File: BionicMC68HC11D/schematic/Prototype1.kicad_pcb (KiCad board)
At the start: 2 copper layers, 48.3 x 71.1 mm, 16 parts, among them J1 BionicConnector, U1 MC68HC11D0P, U2 74HCT126

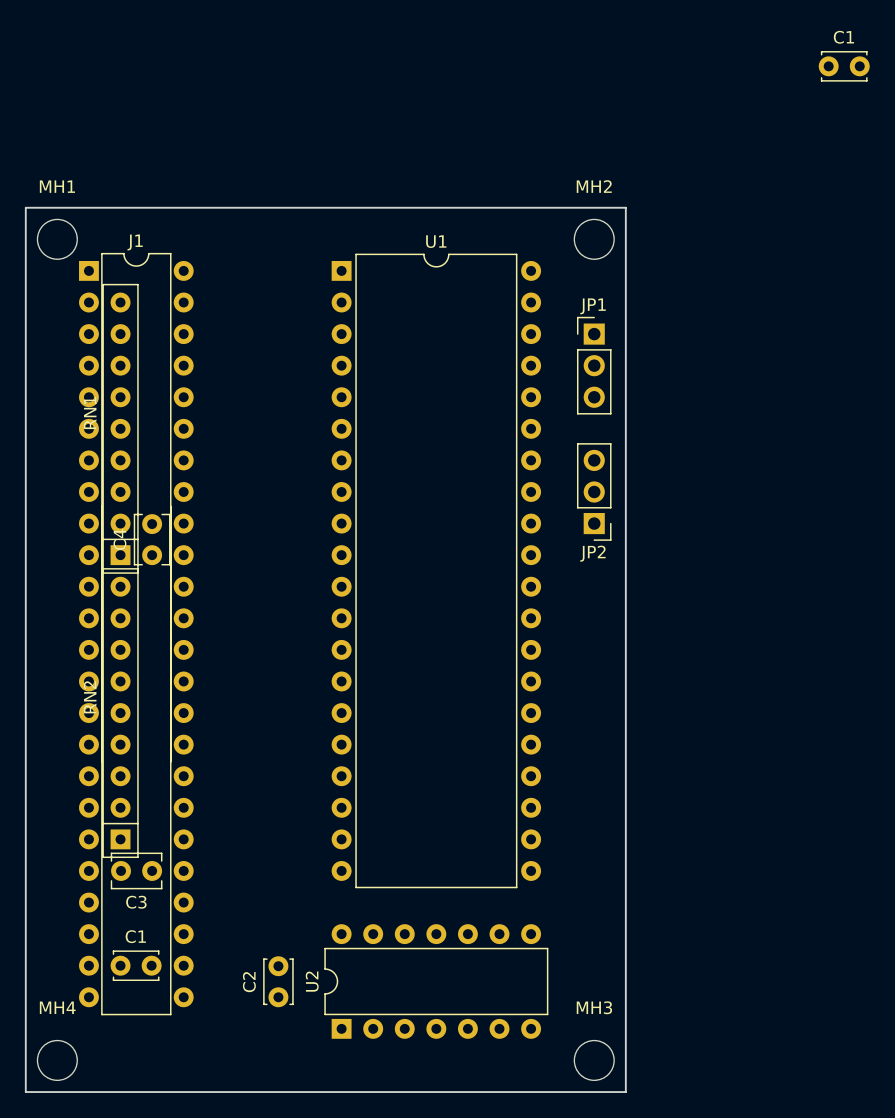
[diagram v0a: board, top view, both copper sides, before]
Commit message: Fix Bionic connector pin outs
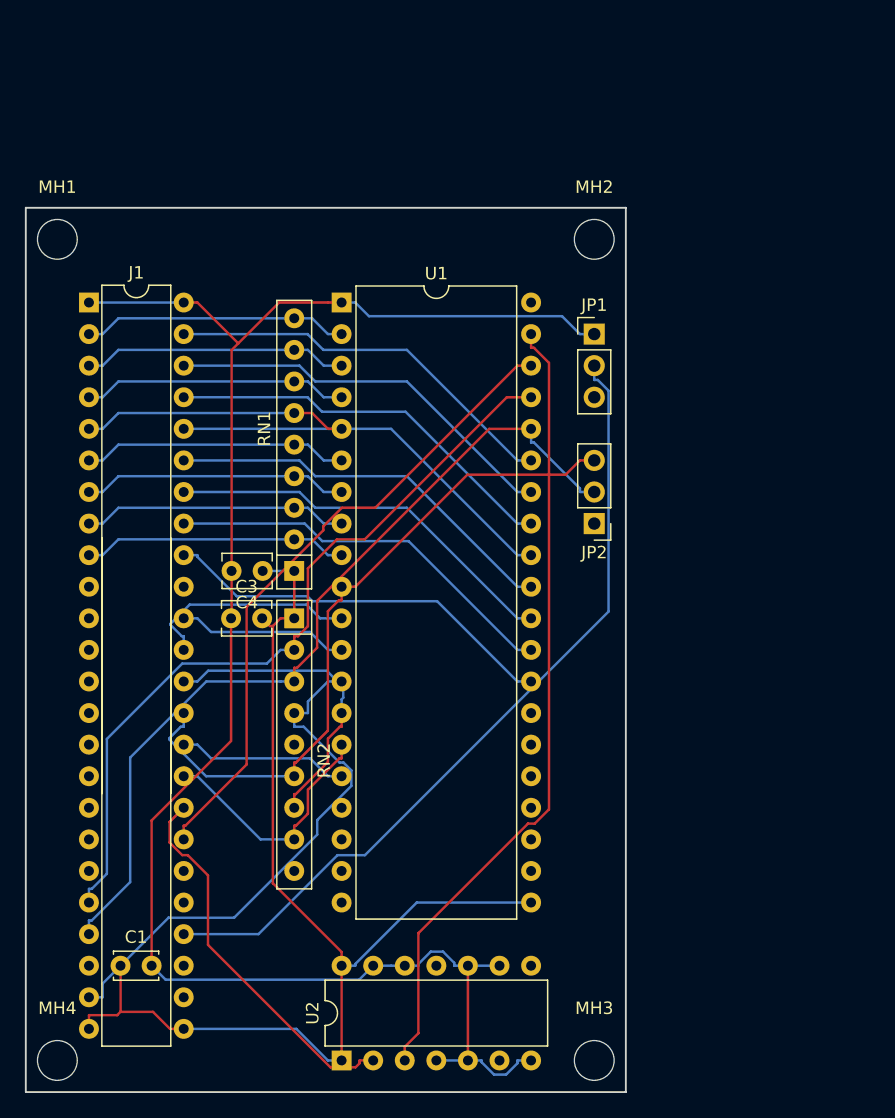
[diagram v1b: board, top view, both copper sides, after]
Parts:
- removed the C1 at (163.0, 56.1)
- removed C2: 0.1u, Capacitor_THT:C_Disc_D3.4mm_W2.1mm_P2.50mm
- moved RN2 22.6 mm to (120.0, 100.5), turned to 270 degrees
- moved C3 21.3 mm to (115.0, 100.5), turned to 0 degrees
- moved RN1 14.0 mm to (120.0, 96.7)
- moved C4 8.98 mm to (117.5, 96.7), turned to 180 degrees
- moved J1 2.54 mm to (103.5, 75.1)
- moved U1 2.54 mm to (123.9, 75.1)
- moved U2 2.54 mm to (123.9, 136.0)
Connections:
- J1 pad 11: /P20 -> Net-(J1-Pad11)
- J1 pad 12: /P21 -> Net-(J1-Pad12)
- J1 pad 13: /P22 -> Net-(J1-Pad13)
- J1 pad 14: /P23 -> Net-(J1-Pad14)
- J1 pad 15: /P24 -> Net-(J1-Pad15)
- J1 pad 16: /P25 -> Net-(J1-Pad16)
- J1 pad 17: /P26 -> Net-(J1-Pad17)
- J1 pad 18: /P27 -> Net-(J1-Pad18)
- J1 pad 40: Net-(J1-Pad40) -> /P27
- J1 pad 41: Net-(J1-Pad41) -> /P26
- J1 pad 42: Net-(J1-Pad42) -> /P25
- J1 pad 43: Net-(J1-Pad43) -> /P24
- J1 pad 44: Net-(J1-Pad44) -> /P23
- J1 pad 45: Net-(J1-Pad45) -> /P22
- J1 pad 46: Net-(J1-Pad46) -> /P21
- J1 pad 47: Net-(J1-Pad47) -> /P20
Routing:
- net GND: track 0.00 -> 143.8 mm
- net VCC: track 0.00 -> 91.0 mm
- net /P51: track 0.00 -> 69.7 mm
- net Net-(J1-Pad28): track 0.00 -> 65.3 mm
- net Net-(U1-Pad39): track 0.00 -> 64.3 mm
- net /P50: track 0.00 -> 62.8 mm
- net /P43: track 0.00 -> 55.6 mm
- net /P47: track 0.00 -> 52.0 mm
- net /P53: track 0.00 -> 43.3 mm
- net /P27: track 0.00 -> 32.2 mm
- net /P25: track 0.00 -> 32.1 mm
- net /P23: track 0.00 -> 32.1 mm
- net /P24: track 0.00 -> 32.1 mm
- net /P20: track 0.00 -> 32.1 mm
- net /P26: track 0.00 -> 32.1 mm
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
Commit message: Migrate to KiCad 6.0
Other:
- net class Default removed
